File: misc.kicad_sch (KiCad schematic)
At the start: 123 parts, among them CN2 Expansion, CN3 Cartridge, CN5 1P, CN504 AV Out, CN6 1P, IC401 74ACT241, IC513 MC34063AM, IC514 L7805, IC701 PIC16F630/18324, IC901 TL974, J1 Barrel_Jack, J2 EXT, Q1 MMBT3904, U1 TPS564257DRLR, U4 L7805

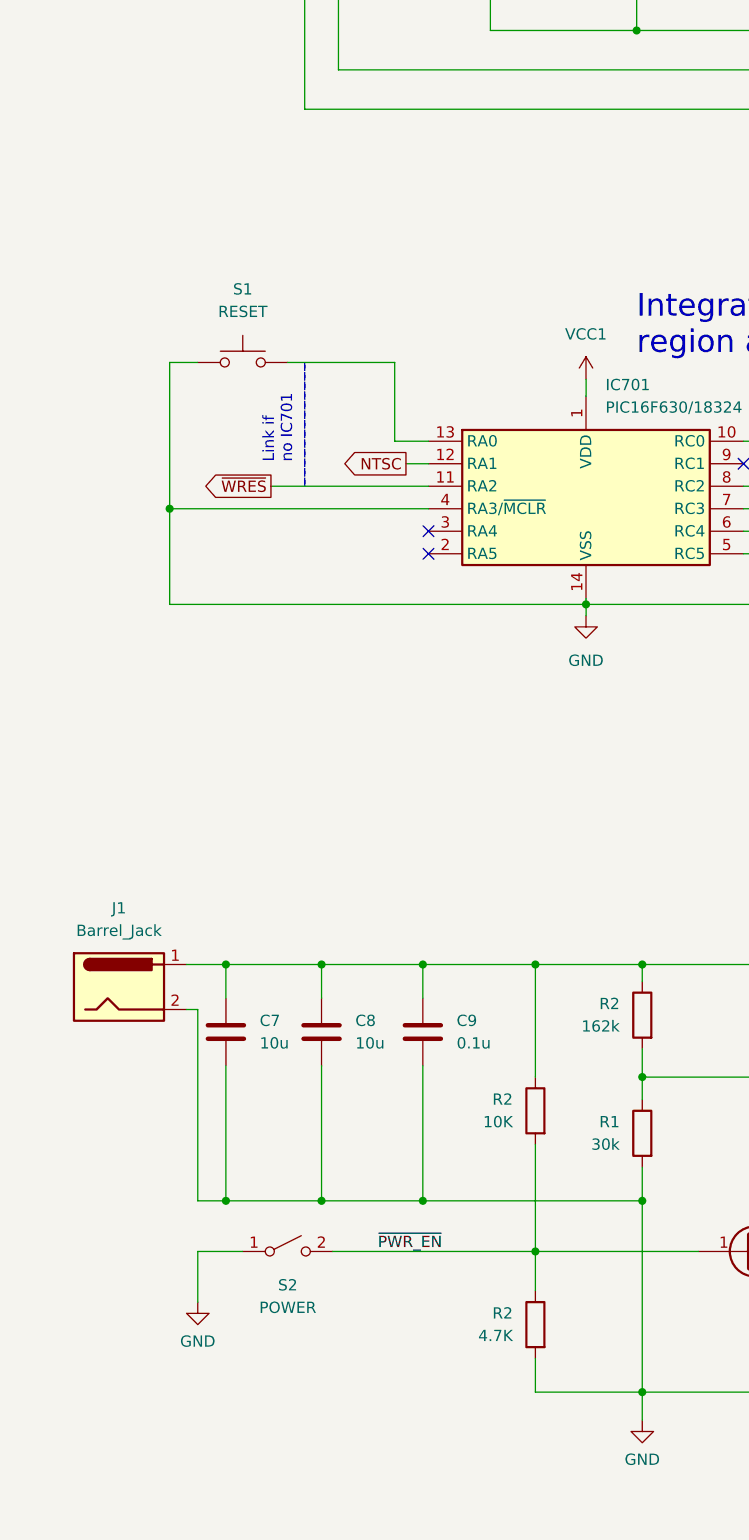
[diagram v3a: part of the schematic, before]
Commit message: Additional power/reset switches for Neptune case.
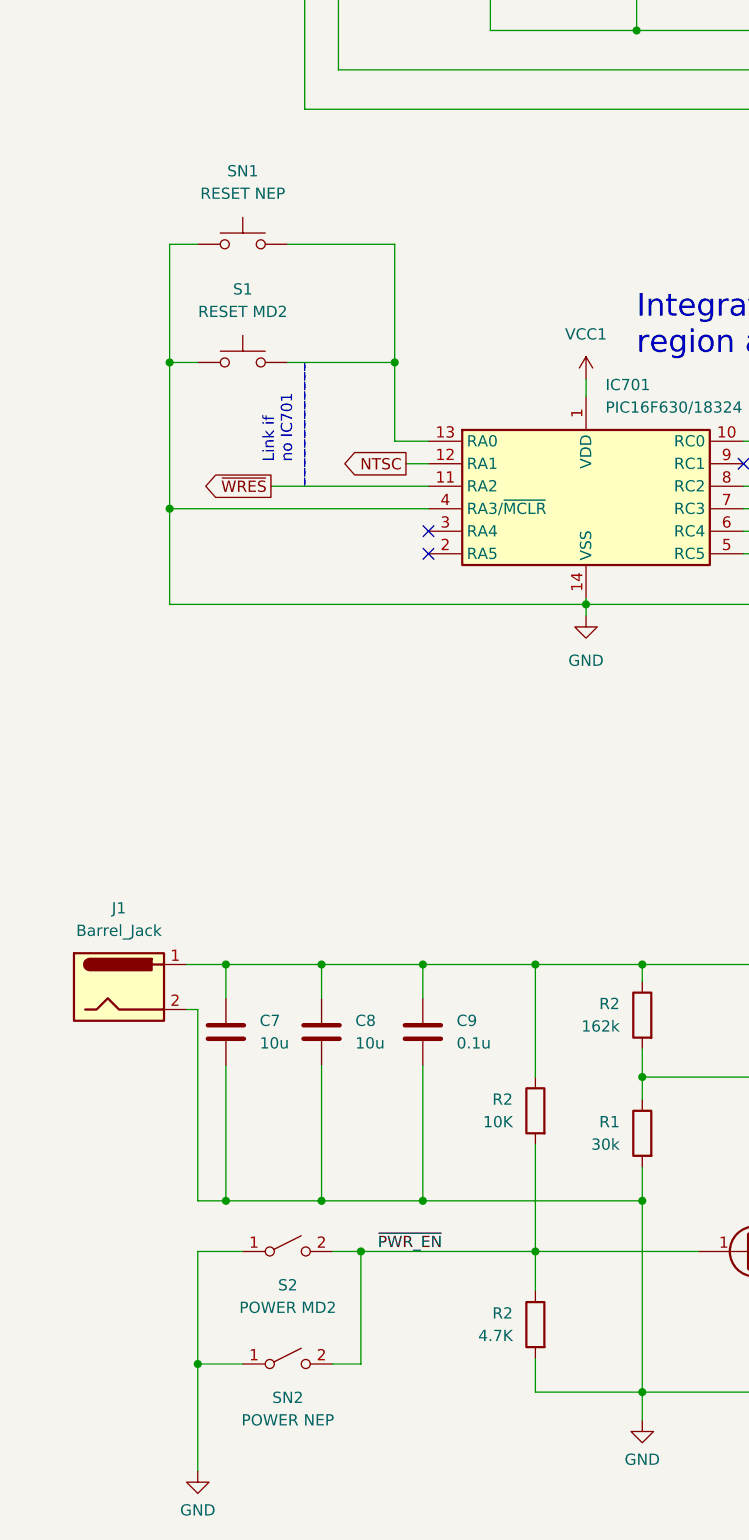
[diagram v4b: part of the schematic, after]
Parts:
- added SN1: RESET NEP, Neptune:Reset_Switch, symbol Switch:SW_Push
- added SN2: POWER NEP, Neptune:Power_Switch, symbol Switch:SW_SPST
- S1: value RESET -> RESET MD2
- S2: value POWER -> POWER MD2
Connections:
- net GND: now also SN1.1, SN2.1 (A)
- net ~{PWR_EN}: now also SN2.2 (B)
- net at IC701.13 (RA0), S1.2: now also SN1.2
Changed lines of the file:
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@@
   (junction (at 528.32 175.895) (diameter 0) (color 0 0 0 0)
   )
+  (junction (at 230.505 246.38) (diameter 0) (color 0 0 0 0)
+  )
   (junction (at 353.06 40.64) (diameter 0) (color 0 0 0 0)
   )
@@
   (junction (at 83.82 233.045) (diameter 0) (color 0 0 0 0)
   )
-  (junction (at 358.14 119.38) (diameter 0) (color 0 0 0 0)
-  )
   (junction (at 221.615 246.38) (diameter 0) (color 0 0 0 0)
   )
+  (junction (at 358.14 119.38) (diameter 0) (color 0 0 0 0)
+  )
   (junction (at 146.05 220.345) (diameter 0) (color 0 0 0 0)
   )
@@
   (junction (at 484.505 147.955) (diameter 0) (color 0 0 0 0)
   )
-  (junction (at 230.505 210.82) (diameter 0) (color 0 0 0 0)
-  )
   (junction (at 83.82 247.015) (diameter 0) (color 0 0 0 0)
   )
@@
   (junction (at 290.83 74.295) (diameter 0) (color 0 0 0 0)
   )
+  (junction (at 33.655 265.43) (diameter 0) (color 0 0 0 0)
+  )
   (junction (at 206.375 149.86) (diameter 0) (color 0 0 0 0)
   )
@@
   (junction (at 546.735 184.785) (diameter 0) (color 0 0 0 0)
   )
+  (junction (at 230.505 210.82) (diameter 0) (color 0 0 0 0)
+  )
   (junction (at 99.695 114.935) (diameter 0) (color 0 0 0 0)
   )
@@
   (junction (at 560.07 139.065) (diameter 0) (color 0 0 0 0)
   )
+  (junction (at 55.88 152.4) (diameter 0) (color 0 0 0 0)
+  )
   (junction (at 84.455 29.845) (diameter 0) (color 0 0 0 0)
   )
@@
   (junction (at 343.535 74.295) (diameter 0) (color 0 0 0 0)
   )
-  (junction (at 211.455 210.82) (diameter 0) (color 0 0 0 0)
-  )
   (junction (at 59.055 247.015) (diameter 0) (color 0 0 0 0)
   )
@@
   (junction (at 577.85 95.885) (diameter 0) (color 0 0 0 0)
   )
-  (junction (at 230.505 246.38) (diameter 0) (color 0 0 0 0)
-  )
   (junction (at 592.455 139.065) (diameter 0) (color 0 0 0 0)
   )
@@
   (junction (at 538.48 95.885) (diameter 0) (color 0 0 0 0)
   )
+  (junction (at 52.07 252.73) (diameter 0) (color 0 0 0 0)
+  )
   (junction (at 211.455 220.345) (diameter 0) (color 0 0 0 0)
   )
@@
   (junction (at 560.07 199.39) (diameter 0) (color 0 0 0 0)
   )
+  (junction (at 30.48 152.4) (diameter 0) (color 0 0 0 0)
+  )
   (junction (at 563.88 95.885) (diameter 0) (color 0 0 0 0)
   )
@@
   (junction (at 280.67 266.065) (diameter 0) (color 0 0 0 0)
   )
+  (junction (at 211.455 210.82) (diameter 0) (color 0 0 0 0)
+  )
   (junction (at 211.455 246.38) (diameter 0) (color 0 0 0 0)
   )
@@
     (stroke (width 0) (type default))
   )
+  (wire (pts (xy 43.815 139.065) (xy 55.88 139.065))
+    (stroke (width 0) (type default))
+  )
   (wire (pts (xy 103.505 225.425) (xy 97.79 225.425))
     (stroke (width 0) (type default))
@@
     (stroke (width 0) (type default))
   )
+  (wire (pts (xy 52.07 252.73) (xy 71.755 252.73))
+    (stroke (width 0) (type default))
+  )
   (wire (pts (xy 349.885 238.125) (xy 353.695 238.125))
     (stroke (width 0) (type default))
@@
     (stroke (width 0) (type default))
   )
-  (wire (pts (xy 211.455 210.82) (xy 230.505 210.82))
+  (wire (pts (xy 177.8 236.855) (xy 177.8 246.38))
     (stroke (width 0) (type default))
   )
-  (wire (pts (xy 177.8 236.855) (xy 177.8 246.38))
+  (wire (pts (xy 48.895 265.43) (xy 52.07 265.43))
     (stroke (width 0) (type default))
   )
@@
     (stroke (width 0) (type default))
   )
+  (wire (pts (xy 33.655 265.43) (xy 38.735 265.43))
+    (stroke (width 0) (type default))
+  )
   (wire (pts (xy 95.25 171.45) (xy 99.06 171.45))
     (stroke (width 0) (type default))
@@
     (stroke (width 0) (type default))
   )
+  (wire (pts (xy 30.48 139.065) (xy 33.655 139.065))
+    (stroke (width 0) (type default))
+  )
   (wire (pts (xy 83.82 247.015) (xy 83.82 268.605))
     (stroke (width 0) (type default))
@@
     (stroke (width 0) (type default))
   )
-  (wire (pts (xy 221.615 246.38) (xy 230.505 246.38))
+  (wire (pts (xy 524.51 85.725) (xy 538.48 85.725))
     (stroke (width 0) (type default))
   )
-  (wire (pts (xy 524.51 85.725) (xy 538.48 85.725))
+  (wire (pts (xy 211.455 210.82) (xy 230.505 210.82))
     (stroke (width 0) (type default))
   )
@@
     (stroke (width 0) (type default))
   )
+  (wire (pts (xy 33.655 265.43) (xy 33.655 252.73))
+    (stroke (width 0) (type default))
+  )
   (wire (pts (xy 604.52 76.2) (xy 604.52 83.82))
     (stroke (width 0) (type default))
@@
     (stroke (width 0) (type default))
   )
+  (wire (pts (xy 211.455 210.82) (xy 211.455 220.345))
+    (stroke (width 0) (type default))
+  )
   (bus (pts (xy 239.395 135.255) (xy 239.395 132.715))
     (stroke (width 0) (type default))
@@
     (stroke (width 0) (type default))
   )
-  (wire (pts (xy 211.455 210.82) (xy 211.455 220.345))
-    (stroke (width 0) (type default))
-  )
   (wire (pts (xy 619.76 85.725) (xy 619.76 86.995))
     (stroke (width 0) (type default))
@@
     (stroke (width 0) (type default))
   )
-  (wire (pts (xy 33.655 258.445) (xy 33.655 252.73))
+  (wire (pts (xy 33.655 277.495) (xy 33.655 265.43))
     (stroke (width 0) (type default))
   )
@@
     (stroke (width 0) (type default))
   )
-  (wire (pts (xy 48.895 252.73) (xy 71.755 252.73))
+  (wire (pts (xy 48.895 252.73) (xy 52.07 252.73))
     (stroke (width 0) (type default))
   )
@@
     (stroke (width 0) (type default))
   )
+  (wire (pts (xy 30.48 152.4) (xy 30.48 139.065))
+    (stroke (width 0) (type default))
+  )
   (wire (pts (xy 148.59 46.99) (xy 148.59 51.435))
     (stroke (width 0) (type default))
@@
     (stroke (width 0) (type default))
   )
+  (wire (pts (xy 55.88 139.065) (xy 55.88 152.4))
+    (stroke (width 0) (type default))
+  )
   (wire (pts (xy 192.405 146.685) (xy 192.405 149.86))
     (stroke (width 0) (type default))
@@
     (stroke (width 0) (type default))
   )
+  (wire (pts (xy 52.07 265.43) (xy 52.07 252.73))
+    (stroke (width 0) (type default))
+  )
   (wire (pts (xy 368.3 210.185) (xy 377.19 210.185))
     (stroke (width 0) (type default))
@@
     (stroke (width 0) (type default))
   )
+  (wire (pts (xy 221.615 246.38) (xy 230.505 246.38))
+    (stroke (width 0) (type default))
+  )
   (wire (pts (xy 539.115 147.955) (xy 539.115 139.065))
     (stroke (width 0) (type default))
@@
       (effects (font (size 1.27 1.27)))
     )
-    (property "Value" "RESET" (at 38.735 146.685 0)
+    (property "Value" "RESET MD2" (at 38.735 146.685 0)
       (effects (font (size 1.27 1.27)))
     )
@@
       (effects (font (size 1.27 1.27)))
     )
-    (property "Value" "POWER" (at 43.815 259.08 0)
+    (property "Value" "POWER MD2" (at 43.815 259.08 0)
       (effects (font (size 1.27 1.27)))
     )
@@
     )
   )
-  (symbol (lib_id "power:GND") (at 33.655 258.445 0) (unit 1)
+  (symbol (lib_id "power:GND") (at 33.655 277.495 0) (unit 1)
     (in_bom yes) (on_board yes) (dnp no) (fields_autoplaced)
-    (property "Reference" "#PWR02" (at 33.655 264.795 0)
+    (property "Reference" "#PWR02" (at 33.655 283.845 0)
       (effects (font (size 1.27 1.27)) hide)
     )
-    (property "Value" "GND" (at 33.655 262.89 0)
+    (property "Value" "GND" (at 33.655 281.94 0)
       (effects (font (size 1.27 1.27)))
     )
-    (property "Footprint" "" (at 33.655 258.445 0)
+    (property "Footprint" "" (at 33.655 277.495 0)
       (effects (font (size 1.27 1.27)) hide)
     )
-    (property "Datasheet" "" (at 33.655 258.445 0)
+    (property "Datasheet" "" (at 33.655 277.495 0)
       (effects (font (size 1.27 1.27)) hide)
     )
@@
     )
   )
+  (symbol (lib_id "Switch:SW_SPST") (at 43.815 265.43 0) (unit 1)
+    (in_bom yes) (on_board yes) (dnp no)
+    (property "Reference" "SN2" (at 43.815 269.24 0)
+      (effects (font (size 1.27 1.27)))
+    )
+    (property "Value" "POWER NEP" (at 43.815 271.78 0)
+      (effects (font (size 1.27 1.27)))
+    )
+    (property "Footprint" "Neptune:Power_Switch" (at 43.815 265.43 0)
+      (effects (font (size 1.27 1.27)) hide)
+    )
+    (property "Datasheet" "~" (at 43.815 265.43 0)
+      (effects (font (size 1.27 1.27)) hide)
+    )
+    (pin "1")
+    (pin "2")
+    (instances
+      (project "Neptune"
+        (path "/bcc23b51-b742-4ae5-9dd6-d96a24058944/01513199-62c5-4123-a151-ccd381a5e6c1"
+          (reference "SN2") (unit 1)
+        )
+      )
+    )
+  )
   (symbol (lib_id "32X:GNDA2") (at 307.34 147.955 0) (unit 1)
     (in_bom yes) (on_board yes) (dnp no) (fields_autoplaced)
@@
         )
       )
+    )
+  )
+  (symbol (lib_id "Switch:SW_Push") (at 38.735 139.065 0) (unit 1)
+    (in_bom yes) (on_board yes) (dnp no) (fields_autoplaced)
+    (property "Reference" "SN1" (at 38.735 130.81 0)
+      (effects (font (size 1.27 1.27)))
+    )
+    (property "Value" "RESET NEP" (at 38.735 133.35 0)
+      (effects (font (size 1.27 1.27)))
+    )
+    (property "Footprint" "Neptune:Reset_Switch" (at 38.735 133.985 0)
+      (effects (font (size 1.27 1.27)) hide)
+    )
+    (property "Datasheet" "~" (at 38.735 133.985 0)
+      (effects (font (size 1.27 1.27)) hide)
+    )
+    (pin "1")
+    (pin "2")
+    (instances
+      (project "Neptune"
+        (path "/bcc23b51-b742-4ae5-9dd6-d96a24058944/01513199-62c5-4123-a151-ccd381a5e6c1"
+          (reference "SN1") (unit 1)
+        )
+      )
